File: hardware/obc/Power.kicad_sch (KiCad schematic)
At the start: 68 parts, among them J14 Conn_01x06, Q1 IRLML2803, Q14 IRF7406PbF, Q2 MBT2222ADW1T1, Q3 MBT2222ADW1T1, U17 BQ25883RGER, U21 TPS7A4501DCQT, U4 ADM1176-1ARMZ-R7, U5 TPS54226PWPRPWP14_2P31X2P46-L, U6 LTC4121

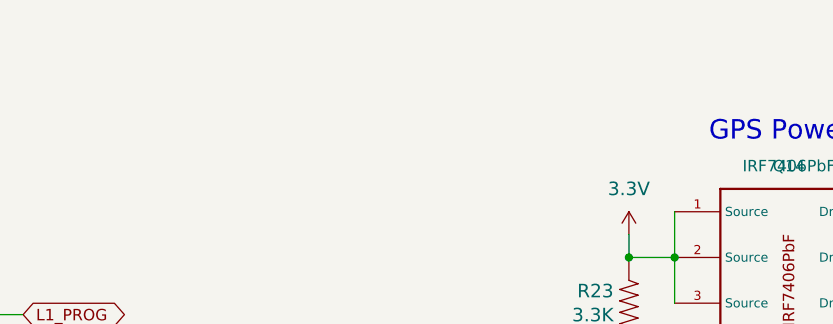
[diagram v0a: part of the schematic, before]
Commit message: obc: Schematic pages to US Letter (except Power)
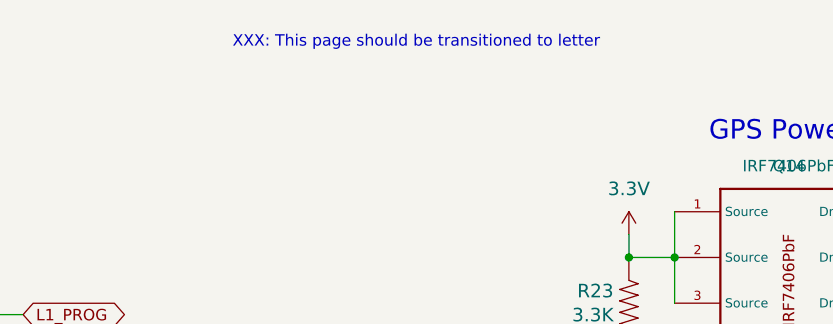
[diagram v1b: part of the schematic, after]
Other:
- note added: "XXX: This page should be transitioned to letter"
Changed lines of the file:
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@@
+		)
+	)
+	(text "XXX: This page should be transitioned to letter"
+		(exclude_from_sim no)
+		(at 210.058 16.764 0)
+		(effects
+			(font
+				(size 1.27 1.27)
+			)
 		)
 	)

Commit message: obc: Add many XXX comments documenting 5/3 review
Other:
- note added: "XXX I think these little "global labels" are silly; We are already connected to net "GND" by the power symbol on the left."
- note added: "XXX calculate these values from OC and maximum power voltages in solar panel design. (4X cells in series, so the voltages will be 4X that of one cell)."
- note added: "XXX consider removing this diode as we have added diodes to the panel assemblies."
- note added: "XXX: This page should be transitioned to letter size, but that requires more shuffling than the rest."
- note removed: "XXX: This page should be transitioned to letter"
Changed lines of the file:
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@@
 	)
 	(junction
-		(at 215.9 60.96)
+		(at 215.9 62.23)
 		(diameter 0)
 		(color 0 0 0 0)
@@
 	(wire
 		(pts
+			(xy 215.9 62.23) (xy 215.9 60.96)
+		)
+		(stroke
+			(width 0)
+			(type default)
+		)
+	)
+	(wire
+		(pts
+			(xy 215.9 63.5) (xy 215.9 62.23)
+		)
+		(stroke
+			(width 0)
+			(type default)
+		)
+	)
+	(wire
+		(pts
 			(xy 161.29 137.16) (xy 161.29 142.24)
 		)
@@
 	(wire
 		(pts
+			(xy 233.68 62.23) (xy 233.68 60.96)
+		)
+		(stroke
+			(width 0)
+			(type default)
+		)
+	)
+	(wire
+		(pts
 			(xy 140.97 46.99) (xy 140.97 44.45)
 		)
@@
 	(wire
 		(pts
-			(xy 233.68 60.96) (xy 215.9 60.96)
+			(xy 233.68 62.23) (xy 215.9 62.23)
 		)
 		(stroke
@@
 		)
 	)
-	(text "XXX: This page should be transitioned to letter"
+	(text "XXX: This page should be transitioned to letter size, but that requires\nmore shuffling than the rest."
 		(exclude_from_sim no)
 		(at 210.058 16.764 0)
@@
 	(text "RF Regulator"
 		(exclude_from_sim no)
-		(at 62.23 87.63 0)
+		(at 62.992 89.154 0)
 		(effects
 			(font
@@
 	(text "XXX: Make accessible from access port"
 		(exclude_from_sim no)
-		(at 246.38 68.58 0)
+		(at 246.38 80.772 0)
 		(effects
 			(font
@@
 		)
 	)
+	(text "XXX calculate these values from\nOC and maximum power voltages in\nsolar panel design.\n\n(4X cells in series, so the voltages\nwill be 4X that of one cell)."
+		(exclude_from_sim no)
+		(at 72.644 78.74 0)
+		(effects
+			(font
+				(size 1.27 1.27)
+			)
+		)
+	)
 	(text "VSOLAR 9V to 40V"
 		(exclude_from_sim no)
@@
 		)
 	)
+	(text "XXX I think these little \"global labels\"\nare silly; We are already connected to net\n\"GND\" by the power symbol on the left."
+		(exclude_from_sim no)
+		(at 240.538 66.294 0)
+		(effects
+			(font
+				(size 1 1)
+			)
+		)
+	)
 	(text "Vfloat=8.4V\n(2S Li-ion)"
 		(exclude_from_sim no)
@@
 		)
 	)
+	(text "XXX consider removing this\ndiode as we have added diodes\nto the panel assemblies."
+		(exclude_from_sim no)
+		(at 29.21 60.198 0)
+		(effects
+			(font
+				(size 1.27 1.27)
+			)
+		)
+	)
 	(label "V_RF"
 		(at 39.37 105.41 0)
@@
 	(global_label "GND"
 		(shape bidirectional)
-		(at 233.68 60.96 180)
+		(at 233.68 62.23 0)
 		(effects
 			(font
 				(size 0.254 0.254)
 			)
-			(justify right)
+			(justify left)
 		)
 		(property "Intersheetrefs" "${INTERSHEET_REFS}"
-			(at 233.68 60.96 0)
+			(at 233.68 62.23 0)
 			(effects
 				(font
 					(size 1.27 1.27)
 				)
+				(justify left)
 				(hide yes)
 			)
@@
 	(symbol
 		(lib_id "mainboard:GND")
-		(at 215.9 63.5 0)
+		(at 215.9 66.04 0)
 		(unit 1)
 		(exclude_from_sim no)
@@
 		(dnp no)
 		(property "Reference" "#GND020"
-			(at 215.9 63.5 0)
+			(at 215.9 66.04 0)
 			(effects
 				(font
@@
 		)
 		(property "Value" "GND"
-			(at 213.36 66.04 0)
+			(at 213.36 68.58 0)
 			(effects
 				(font
@@
 		)
 		(property "Footprint" ""
-			(at 215.9 63.5 0)
+			(at 215.9 66.04 0)
 			(effects
 				(font
@@
 		)
 		(property "Datasheet" ""
-			(at 215.9 63.5 0)
+			(at 215.9 66.04 0)
 			(effects
 				(font
@@
 		)
 		(property "Description" ""
-			(at 215.9 63.5 0)
+			(at 215.9 66.04 0)
 			(effects
 				(font

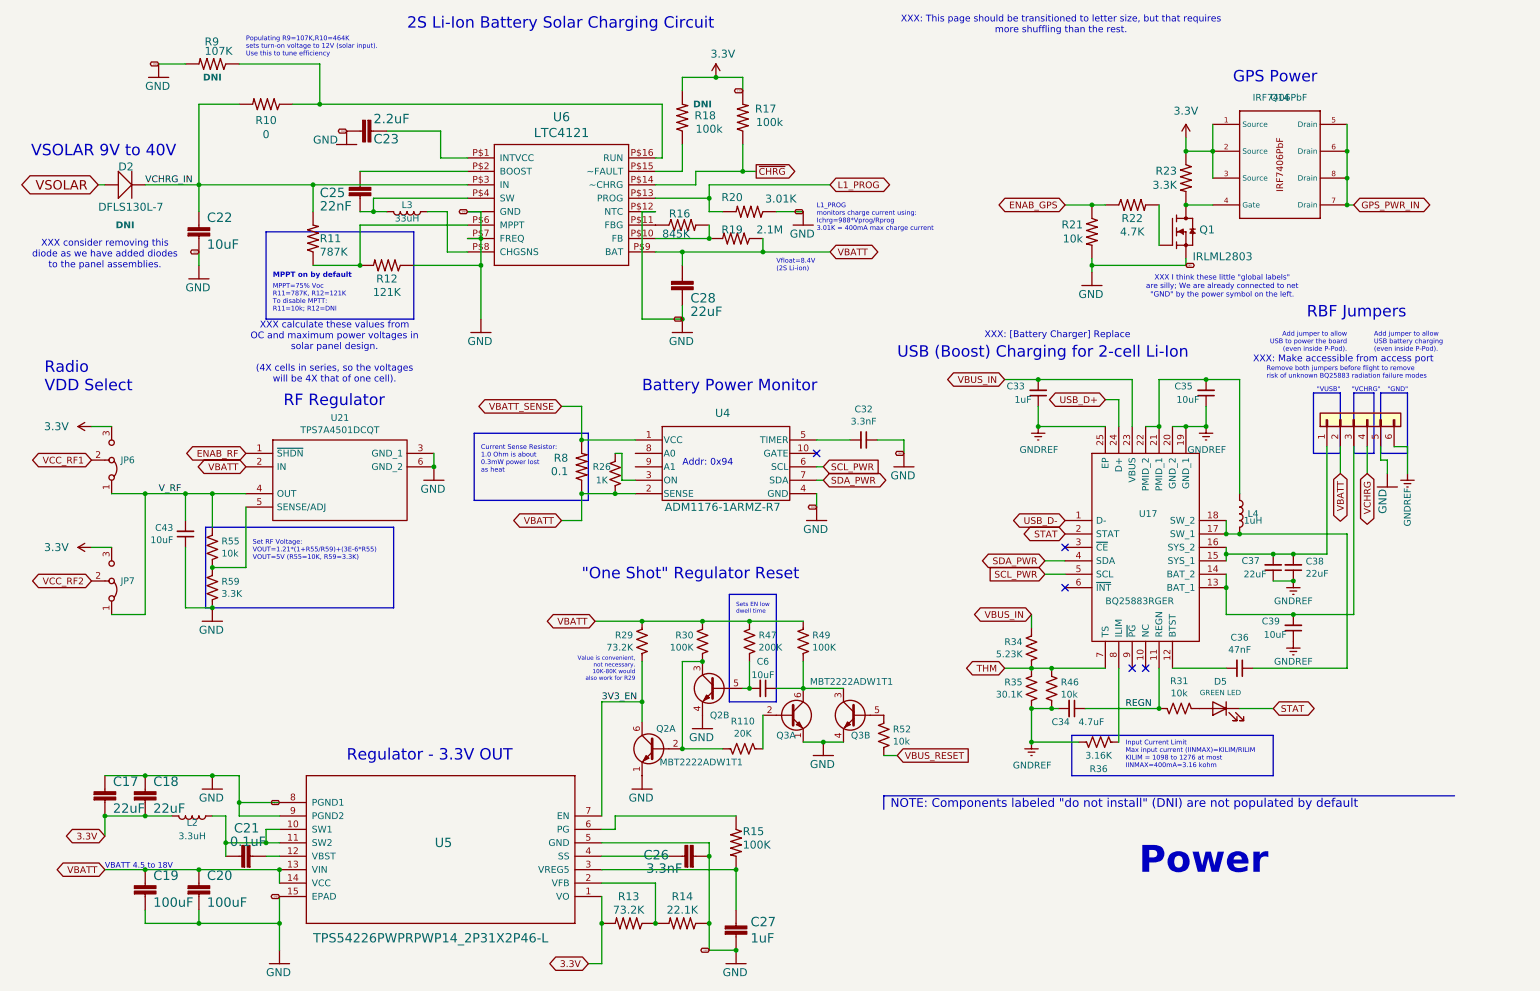
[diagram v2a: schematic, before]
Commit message: obc: schematic editing and footprint development
Deleted irrelevant SD-related circuits and pins. Created new & modified existing connector and inductor footprints. Added new components (Bat Charger, High-Rel Connector, etc.)
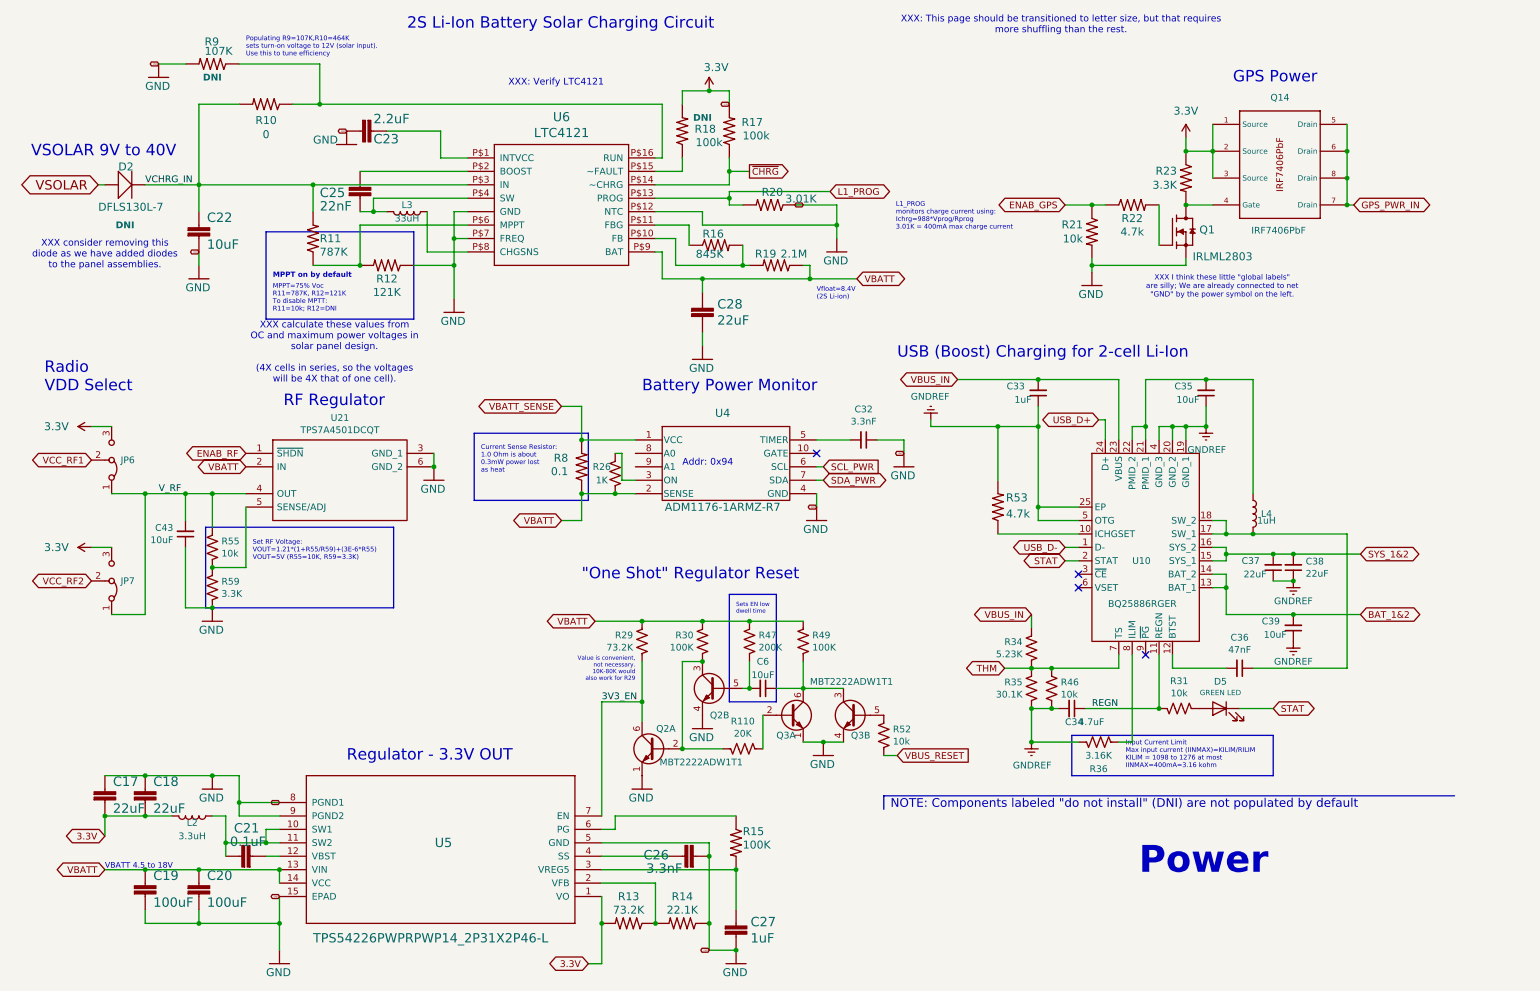
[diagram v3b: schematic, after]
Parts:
- removed J14: Conn_01x06, Connector_PinHeader_2.54mm:PinHeader_1x06_P2.54mm_Vertical, symbol Connector_Generic:Conn_01x06
- removed U17: BQ25883RGER, mainboard:QFN50P400X400X100-25N-D, symbol mainboard:BQ25883RGER
- added R53: 4.7k, Resistor_SMD:R_0603_1608Metric, symbol mainboard:RESISTOR0603
- added U10: BQ25886RGER, symbol SSE_Symbols:BatChrgr_BQ25886RGER
- L2: footprint mainboard:L_2141 -> SSE_Footprints:TDK_1008_2.9x2.0mm
- L3: footprint Inductor_SMD:L_1812_4532Metric -> SSE_Footprints:TDK_1008_4.9x5.5mm
- L4: footprint mainboard:L_2510 -> SSE_Footprints:Murata_1008_2.5x2.0mm
- Q14: footprint (none) -> SSE_Footprints:SO-8_3.9x4.9mm_P1.27mm
- R22: value 4.7K -> 4.7k
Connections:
- net GNDREF: now also R53.2, U10.19 (GND_1), U10.20 (GND_2), U10.25 (EP), U10.4 (GND_3), U10.5 (OTG)
- net REGN: now also U10.11 (REGN)
- net STAT: now also U10.2 (STAT)
- net THM: now also U10.7 (TS)
- net USB_D+: now also U10.24 (D+)
- net USB_D-: now also U10.1 (D-)
- net VBUS_IN: now also U10.23 (VBUS)
- net at C36.1, L4.2: now also U10.17 (SW_1), U10.18 (SW_2)
- net at C36.2: now also U10.12 (BTST)
- net SYS_1&2: now reaches C37.2, C38.2
- net SYS_1&2: now also U10.15 (SYS_1), U10.16 (SYS_2)
- net BAT_1&2: now reaches C39.2
- net BAT_1&2: now also U10.13 (BAT_1), U10.14 (BAT_2)
- net at C35.2, L4.1: now also U10.21 (PMID_1), U10.22 (PMID_2)
- net at R36.2: now also U10.8 (ILIM)
- new net: R53.1, U10.10 (ICHGSET)
- no-connect marks 5 -> 4
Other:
- note added: "XXX: Verify LTC4121"
- note removed: ""GND""
- note removed: ""VCHRG""
- note removed: ""VUSB""
- note removed: "Add jumper to allow USB battery charging (even inside P-Pod)."
- note removed: "Add jumper to allow USB to power the board (even inside P-Pod)."
- note removed: "RBF Jumpers"
- note removed: "Remove both jumpers before flight to remove risk of unknown BQ25883 radiation failure modes"
- note removed: "XXX: Make accessible from access port"
- note removed: "XXX: [Battery Charger] Replace"
- moved on the sheet: C28, L4, R16, R17, R18, R19, R20

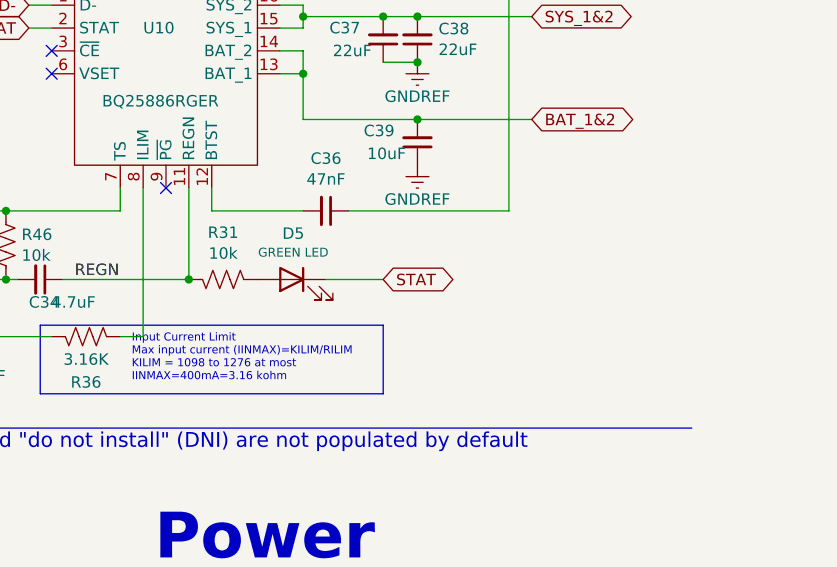
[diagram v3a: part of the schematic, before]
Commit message: obc: BOM component verification
Verified part numbers, availability, values, footprints, etc. of components. Next steps involve verifying footprints and potentially researching some alternative components.
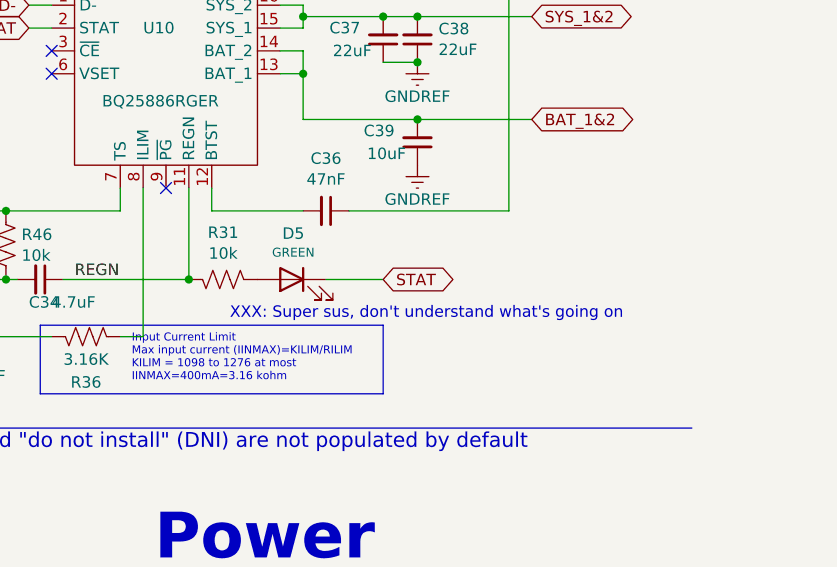
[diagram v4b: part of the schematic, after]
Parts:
- C17, C18, C22, C28, C34, C35, C37, C38, C39, C43, C6: Notes (none) -> 10V ok?
- C19, C20: LCSC C2180446 -> C90143; Manufacturer_Name Kyocera AVX -> Taiyo Yuden; Manufacturer_Part_Number 1210YD107MAT2A -> EMK325ABJ107MM-P; Notes (none) -> 16V ok?
- C27, C33: Manufacturer_Name (none) -> Samsung Electro-Mechanics; Manufacturer_Part_Number (none) -> CL10B105KO8NNNC; Notes (none) -> 16V ok?
- D5: value GREEN LED -> GREEN
- L2: Notes 3.3uH for 3V3 switching -> Footprint Marked as Issue - 3.3uH for 3V3 switching
- L3: Notes 33uH for solar charging, kinda big -> Footprint Marked as Issue - 33uH for solar charging, kinda 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
- L4: Notes 1uH for USB charging -> Footprint Marked as Issue - 1uH for USB charging
- Q1: footprint mainboard:SOT-23 -> Package_TO_SOT_SMD:SOT-23
- Q14: footprint SSE_Footprints:SO-8_3.9x4.9mm_P1.27mm -> Package_SO:SO-8_3.9x4.9mm_P1.27mm
- R12: LCSC C2992526 -> C861095; Manufacturer_Name Vishay Intertech -> YAGEO; Manufacturer_Part_Number TNPW0603121KBEEA -> RT0603BRD07121KL
- R14: LCSC C844759 -> C2838732; Manufacturer_Name Vishay Intertech -> YAGEO; Manufacturer_Part_Number CRCW060322K1FKEA -> AF0603FR-0722K1L
- R35: LCSC C844775 -> C137745; Manufacturer_Name Vishay Intertech -> YAGEO; Manufacturer_Part_Number CRCW060330K1FKEA -> RC0603FR-0730K1L
- U10: footprint (none) -> mainboard:QFN50P400X400X100-25N-D; Manufacturer_Name (none) -> Texas Instruments; Manufacturer_Part_Number (none) -> BQ25886RGER; Notes footprint in mainboard files -> (none)
- U21: footprint mainboard:TPS7A4501DCQT -> Package_TO_SOT_SMD:SOT-223-6
- U4: LCSC NotAvailable -> C657860; Notes Marked as issue, unsure -> Consigned parts to JLCPCB.
- U5: footprint mainboard:PWP14_2P31X2P46-L -> Package_SO:HTSSOP-14-1EP_4.4x5mm_P0.65mm_EP3.4x5mm_Mask3x3.1mm
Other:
- note added: "XXX: Super sus, don't understand what's going on"
